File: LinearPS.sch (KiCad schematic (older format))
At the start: 100 parts, among them J1 Conn_01x03, J10 Conn_01x01, J11 Conn_01x01, J12 Conn_01x01, J14 Conn_01x01, J2 Conn_01x02, J3 Conn_01x03, J4 Conn_01x01, J5 Conn_01x01, J6 Conn_01x01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

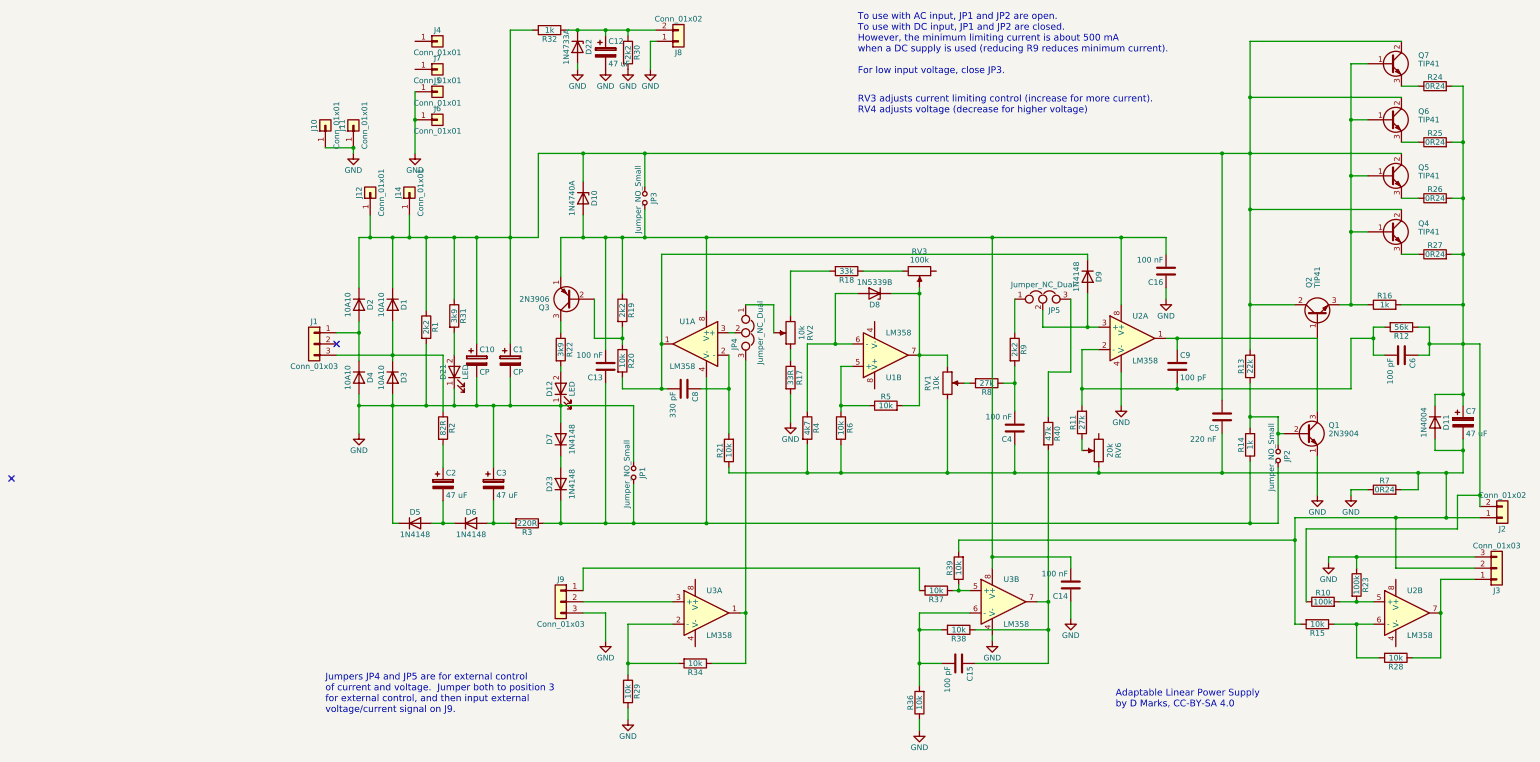
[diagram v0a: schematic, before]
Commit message: Fixed several layout issues, added a couple of resistors to ensure stability
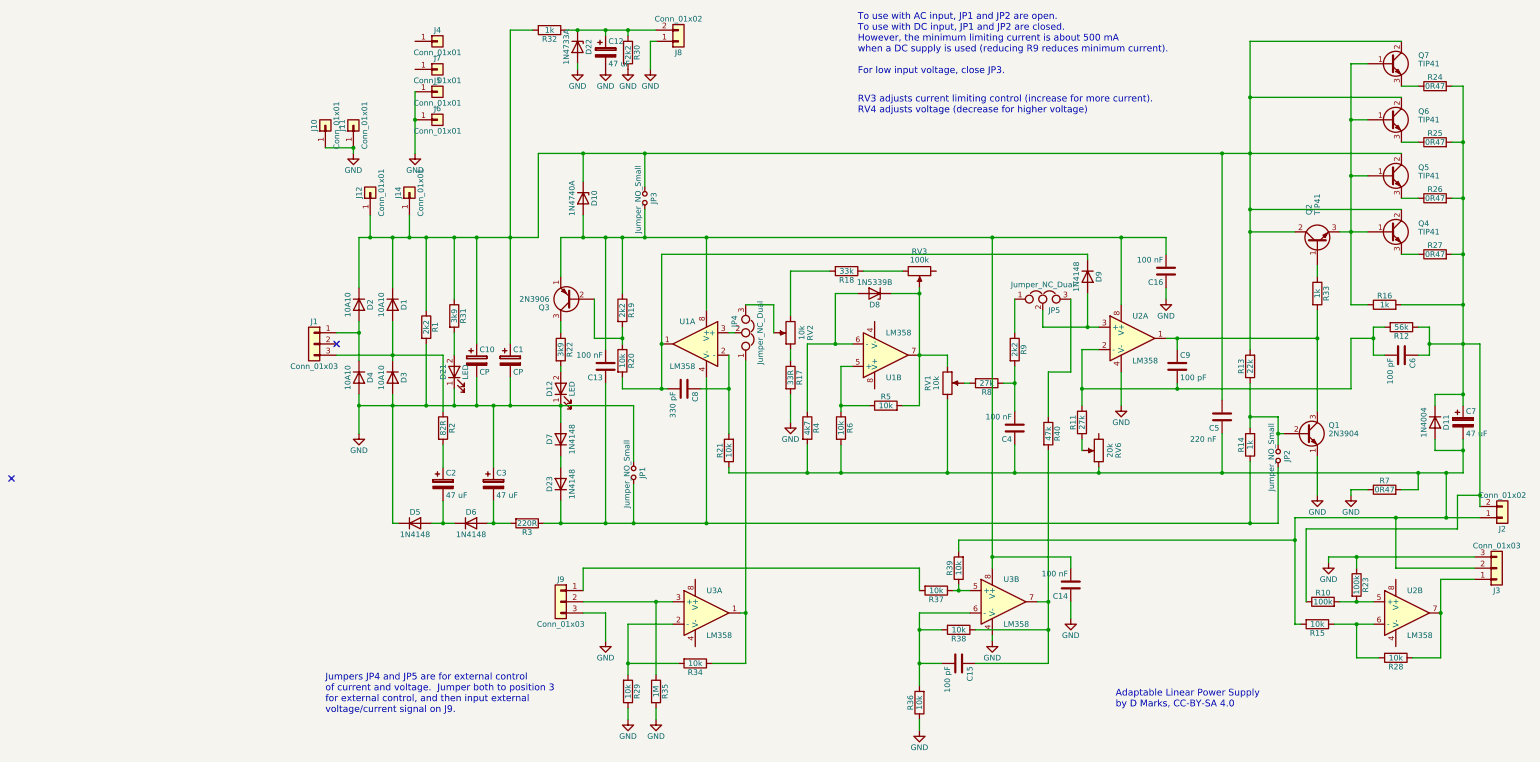
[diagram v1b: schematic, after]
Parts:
- added R33: 1k, Resistors_THT:R_Axial_DIN0411_L9.9mm_D3.6mm_P12.70mm_Horizontal, symbol R
- added R35: 1M, Resistors_THT:R_Axial_DIN0207_L6.3mm_D2.5mm_P7.62mm_Horizontal, symbol R
- R24, R25, R26, R27, R7: value 0R24 -> 0R47
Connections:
- net GND: now also R29.1, R35.2; no longer R29.2
- net at RV2.2: now also JP4.3; no longer JP4.1
- net at C9.1, Q1.3 (C), U2.1: now also R33.2; no longer Q2.1 (B)
- net at R34.1, U3.1: now also JP4.1; no longer JP4.3
- net at R34.2, U3.2 (-): now also R29.2; no longer R29.1
- net at J9.2 (Pin_2), U3.3 (+): now also R35.1
- new net: Q2.1 (B), R33.1
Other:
- moved on the sheet: Q2
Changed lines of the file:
@@
 $EndComp
 $Comp
-L GND #PWR01
+L GND #PWR2
 U 1 1 5CEC838A
 P 950 4450
-F 0 "#PWR01" H 950 4200 50  0001 C CNN
+F 0 "#PWR2" H 950 4200 50  0001 C CNN
 F 1 "GND" H 950 4300 50  0000 C CNN
 F 2 "" H 950 4450 50  0001 C CNN
@@
 L TIP41 Q2
 U 1 1 5CED0A73
-P 9500 3400
-F 0 "Q2" H 9750 3475 50  0000 L CNN
-F 1 "TIP41" H 9750 3400 50  0000 L CNN
-F 2 "linearps:TO-220-3_Vertical_WithPads" H 9750 3325 50  0001 L CIN
-F 3 "" H 9500 3400 50  0001 L CNN
-	1    9500 3400
+P 9500 2750
+F 0 "Q2" H 9750 2825 50  0000 L CNN
+F 1 "TIP41" H 9750 2750 50  0000 L CNN
+F 2 "linearps:TO-220-3_Vertical_WithPads" H 9750 2675 50  0001 L CIN
+F 3 "" H 9500 2750 50  0001 L CNN
+	1    9500 2750
 	0    -1   -1   0
 $EndComp
@@
 P 10100 4950
 F 0 "R7" V 10180 4950 50  0000 C CNN
-F 1 "0R24" V 10100 4950 50  0000 C CNN
+F 1 "0R47" V 10100 4950 50  0000 C CNN
 F 2 "Resistors_THT:R_Axial_Power_L25.0mm_W6.4mm_P27.94mm" V 10030 4950 50  0001 C CNN
 F 3 "" H 10100 4950 50  0001 C CNN
@@
 P 10550 1350
 F 0 "R24" V 10630 1350 50  0000 C CNN
-F 1 "0R24" V 10550 1350 50  0000 C CNN
+F 1 "0R47" V 10550 1350 50  0000 C CNN
 F 2 "Resistors_THT:R_Axial_Power_L25.0mm_W6.4mm_P27.94mm" V 10480 1350 50  0001 C CNN
 F 3 "" H 10550 1350 50  0001 C CNN
@@
 P 10550 1850
 F 0 "R25" V 10630 1850 50  0000 C CNN
-F 1 "0R24" V 10550 1850 50  0000 C CNN
+F 1 "0R47" V 10550 1850 50  0000 C CNN
 F 2 "Resistors_THT:R_Axial_Power_L25.0mm_W6.4mm_P27.94mm" V 10480 1850 50  0001 C CNN
 F 3 "" H 10550 1850 50  0001 C CNN
@@
 P 10550 2350
 F 0 "R26" V 10630 2350 50  0000 C CNN
-F 1 "0R24" V 10550 2350 50  0000 C CNN
+F 1 "0R47" V 10550 2350 50  0000 C CNN
 F 2 "Resistors_THT:R_Axial_Power_L25.0mm_W6.4mm_P27.94mm" V 10480 2350 50  0001 C CNN
 F 3 "" H 10550 2350 50  0001 C CNN
@@
 P 10550 2850
 F 0 "R27" V 10630 2850 50  0000 C CNN
-F 1 "0R24" V 10550 2850 50  0000 C CNN
+F 1 "0R47" V 10550 2850 50  0000 C CNN
 F 2 "Resistors_THT:R_Axial_Power_L25.0mm_W6.4mm_P27.94mm" V 10480 2850 50  0001 C CNN
 F 3 "" H 10550 2850 50  0001 C CNN
@@
 $EndComp
 $Comp
-L GND #PWR02
+L GND #PWR4
 U 1 1 5CECFA19
 P 2900 1200
-F 0 "#PWR02" H 2900 950 50  0001 C CNN
+F 0 "#PWR4" H 2900 950 50  0001 C CNN
 F 1 "GND" H 2900 1050 50  0000 C CNN
 F 2 "" H 2900 1200 50  0001 C CNN
@@
 $EndComp
 $Comp
-L GND #PWR03
+L GND #PWR9
 U 1 1 5CED04A2
 P 3550 1200
-F 0 "#PWR03" H 3550 950 50  0001 C CNN
+F 0 "#PWR9" H 3550 950 50  0001 C CNN
 F 1 "GND" H 3550 1050 50  0000 C CNN
 F 2 "" H 3550 1200 50  0001 C CNN
@@
 $EndComp
 $Comp
-L GND #PWR04
+L GND #PWR5
 U 1 1 5CED0ACE
 P 3150 1200
-F 0 "#PWR04" H 3150 950 50  0001 C CNN
+F 0 "#PWR5" H 3150 950 50  0001 C CNN
 F 1 "GND" H 3150 1050 50  0000 C CNN
 F 2 "" H 3150 1200 50  0001 C CNN
@@
 $EndComp
 $Comp
-L GND #PWR05
+L GND #PWR7
 U 1 1 5CED1C83
 P 3350 1200
-F 0 "#PWR05" H 3350 950 50  0001 C CNN
+F 0 "#PWR7" H 3350 950 50  0001 C CNN
 F 1 "GND" H 3350 1050 50  0000 C CNN
 F 2 "" H 3350 1200 50  0001 C CNN
@@
 $EndComp
 $Comp
-L GND #PWR06
+L GND #PWR13
 U 1 1 5D2A363C
 P 6600 6300
-F 0 "#PWR06" H 6600 6050 50  0001 C CNN
+F 0 "#PWR13" H 6600 6050 50  0001 C CNN
 F 1 "GND" H 6600 6150 50  0000 C CNN
 F 2 "" H 6600 6300 50  0001 C CNN
@@
 $EndComp
 $Comp
-L GND #PWR07
+L GND #PWR12
 U 1 1 5D2A4408
 P 5950 7100
-F 0 "#PWR07" H 5950 6850 50  0001 C CNN
+F 0 "#PWR12" H 5950 6850 50  0001 C CNN
 F 1 "GND" H 5950 6950 50  0000 C CNN
 F 2 "" H 5950 7100 50  0001 C CNN
@@
 $EndComp
 $Comp
-L GND #PWR08
+L GND #PWR6
 U 1 1 5D2A5B2D
 P 3150 6300
-F 0 "#PWR08" H 3150 6050 50  0001 C CNN
+F 0 "#PWR6" H 3150 6050 50  0001 C CNN
 F 1 "GND" H 3150 6150 50  0000 C CNN
 F 2 "" H 3150 6300 50  0001 C CNN
@@
 $EndComp
 $Comp
-L GND #PWR09
+L GND #PWR14
 U 1 1 5D2A7B6A
 P 7300 6100
-F 0 "#PWR09" H 7300 5850 50  0001 C CNN
+F 0 "#PWR14" H 7300 5850 50  0001 C CNN
 F 1 "GND" H 7300 5950 50  0000 C CNN
 F 2 "" H 7300 6100 50  0001 C CNN
@@
 F 3 "" H 4400 3550 50  0001 C CNN
 	1    4400 3550
-	0    1    1    0
+	0    1    -1   0
 $EndComp
 Text Notes 650  6950 0    60   ~ 0
@@
 $EndComp
 $Comp
-L GND #PWR010
+L GND #PWR8
 U 1 1 5D2A7293
 P 3350 7000
-F 0 "#PWR010" H 3350 6750 50  0001 C CNN
+F 0 "#PWR8" H 3350 6750 50  0001 C CNN
 F 1 "GND" H 3350 6850 50  0000 C CNN
 F 2 "" H 3350 7000 50  0001 C CNN
@@
 F 3 "" H 3350 6750 50  0001 C CNN
 	1    3350 6750
-	1    0    0    -1
+	1    0    0    1
 $EndComp
 $Comp
@@
 $EndComp
 $Comp
-L GND #PWR011
+L GND #PWR3
 U 1 1 5D2BE3B3
 P 1450 1950
-F 0 "#PWR011" H 1450 1700 50  0001 C CNN
+F 0 "#PWR3" H 1450 1700 50  0001 C CNN
 F 1 "GND" H 1450 1800 50  0000 C CNN
 F 2 "" H 1450 1950 50  0001 C CNN
@@
 $EndComp
 $Comp
-L GND #PWR012
+L GND #PWR16
 U 1 1 5D5FCB6F
 P 8150 3250
-F 0 "#PWR012" H 8150 3000 50  0001 C CNN
+F 0 "#PWR16" H 8150 3000 50  0001 C CNN
 F 1 "GND" H 8150 3100 50  0000 C CNN
 F 2 "" H 8150 3250 50  0001 C CNN
@@
 $EndComp
 $Comp
-L GND #PWR013
+L GND #PWR18
 U 1 1 5D5FFE57
 P 9600 5600
-F 0 "#PWR013" H 9600 5350 50  0001 C CNN
+F 0 "#PWR18" H 9600 5350 50  0001 C CNN
 F 1 "GND" H 9600 5450 50  0000 C CNN
 F 2 "" H 9600 5600 50  0001 C CNN
@@
 $EndComp
 $Comp
-L GND #PWR014
+L GND #PWR11
 U 1 1 5D606C21
 P 4800 4350
-F 0 "#PWR014" H 4800 4100 50  0001 C CNN
+F 0 "#PWR11" H 4800 4100 50  0001 C CNN
 F 1 "GND" H 4800 4200 50  0000 C CNN
 F 2 "" H 4800 4350 50  0001 C CNN
@@
 $EndComp
 $Comp
-L GND #PWR015
+L GND #PWR15
 U 1 1 5D608020
 P 7750 4200
-F 0 "#PWR015" H 7750 3950 50  0001 C CNN
+F 0 "#PWR15" H 7750 3950 50  0001 C CNN
 F 1 "GND" H 7750 4050 50  0000 C CNN
 F 2 "" H 7750 4200 50  0001 C CNN
@@
 $EndComp
 $Comp
-L GND #PWR016
+L GND #PWR17
 U 1 1 5D608830
 P 9500 5000
-F 0 "#PWR016" H 9500 4750 50  0001 C CNN
+F 0 "#PWR17" H 9500 4750 50  0001 C CNN
 F 1 "GND" H 9500 4850 50  0000 C CNN
 F 2 "" H 9500 5000 50  0001 C CNN
@@
 $EndComp
 $Comp
-L GND #PWR017
+L GND #PWR19
 U 1 1 5D60C78D
 P 9800 5000
-F 0 "#PWR017" H 9800 4750 50  0001 C CNN
+F 0 "#PWR19" H 9800 4750 50  0001 C CNN
 F 1 "GND" H 9800 4850 50  0000 C CNN
 F 2 "" H 9800 5000 50  0001 C CNN
@@
 $EndComp
 $Comp
-L GND #PWR018
+L GND #PWR1
 U 1 1 5D664C72
 P 900 1950
-F 0 "#PWR018" H 900 1700 50  0001 C CNN
+F 0 "#PWR1" H 900 1700 50  0001 C CNN
 F 1 "GND" H 900 1800 50  0000 C CNN
 F 2 "" H 900 1950 50  0001 C CNN
@@
 	1    0    0    -1
 $EndComp
+$Comp
+L R R33
+U 1 1 5D6CB0C3
+P 9500 3200
+F 0 "R33" V 9580 3200 50  0000 C CNN
+F 1 "1k" V 9500 3200 50  0000 C CNN
+F 2 "Resistors_THT:R_Axial_DIN0411_L9.9mm_D3.6mm_P12.70mm_Horizontal" V 9430 3200 50  0001 C CNN
+F 3 "" H 9500 3200 50  0001 C CNN
+	1    9500 3200
+	1    0    0    -1
+$EndComp
 Connection ~ 10650 5200
 Connection ~ 10650 4800
@@
 Wire Wire Line
 	3400 4200 3400 4700
-Connection ~ 8250 3600
 Wire Wire Line
 	9150 4300 8900 4300
@@
 Connection ~ 1700 5250
 Connection ~ 2150 5250
-Connection ~ 9800 3300
 Connection ~ 10800 2850
 Wire Wire Line
@@
 	8900 2450 10250 2450
 Wire Wire Line
-	9700 3300 9950 3300
-Wire Wire Line
-	9800 2650 9950 2650
+	9800 3300 9950 3300
+Wire Wire Line
+	9700 2650 9950 2650
 Wire Wire Line
 	9800 1150 9800 3300
@@
 	9200 4450 9150 4450
 Wire Wire Line
-	9500 3600 9500 4250
+	9500 3350 9500 4250
 Wire Wire Line
 	9500 4650 9500 5000
-Connection ~ 8900 3300
-Wire Wire Line
-	8900 3300 9300 3300
 Wire Wire Line
 	8900 950  8900 3700
@@
 	8150 3600 9500 3600
 Wire Wire Line
-	8250 3700 8250 3600
+	8250 3600 8250 3700
 Connection ~ 6800 4800
 Wire Wire Line
@@
 Wire Wire Line
 	650  1900 900  1900
+Connection ~ 8250 3600
+Wire Wire Line
+	9300 2650 8900 2650
+Connection ~ 8900 2650
+Wire Wire Line
+	9500 2950 9500 3050
+Connection ~ 9500 3600
+$Comp
+L R R35
+U 1 1 5D6D3F55
+P 3600 6750
+F 0 "R35" V 3680 6750 50  0000 C CNN
+F 1 "1M" V 3600 6750 50  0000 C CNN
+F 2 "Resistors_THT:R_Axial_DIN0207_L6.3mm_D2.5mm_P7.62mm_Horizontal" V 3530 6750 50  0001 C CNN
+F 3 "" H 3600 6750 50  0001 C CNN
+	1    3600 6750
+	1    0    0    -1
+$EndComp
+$Comp
+L GND #PWR10
+U 1 1 5D6D40A8
+P 3600 7000
+F 0 "#PWR10" H 3600 6750 50  0001 C CNN
+F 1 "GND" H 3600 6850 50  0000 C CNN
+F 2 "" H 3600 7000 50  0001 C CNN
+F 3 "" H 3600 7000 50  0001 C CNN
+	1    3600 7000
+	1    0    0    -1
+$EndComp
+Wire Wire Line
+	3600 6900 3600 7000
+Wire Wire Line
+	3600 6600 3600 5950
+Connection ~ 3600 5950
 $EndSCHEMATC
